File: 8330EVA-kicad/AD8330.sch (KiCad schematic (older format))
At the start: 20 parts, among them J6 Conn_01x03_Male, T1 T1-1T-KK81, T2 T1-1T-KK81, U3 AD8330

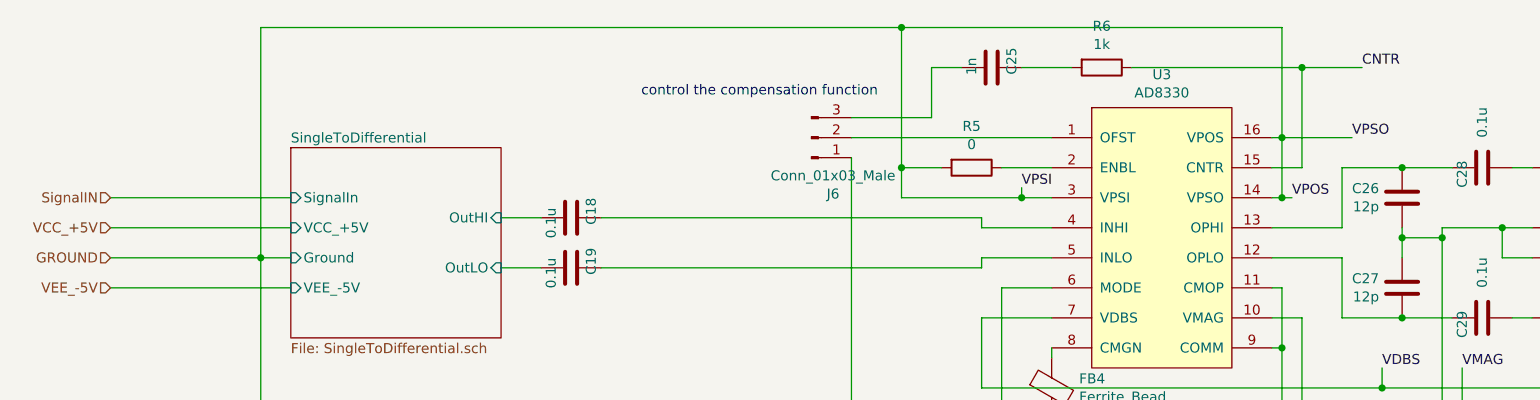
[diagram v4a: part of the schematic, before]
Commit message: 修复AD8330模块中的错误
1.  VCC连接错误
2. VPOS和VPSO标反
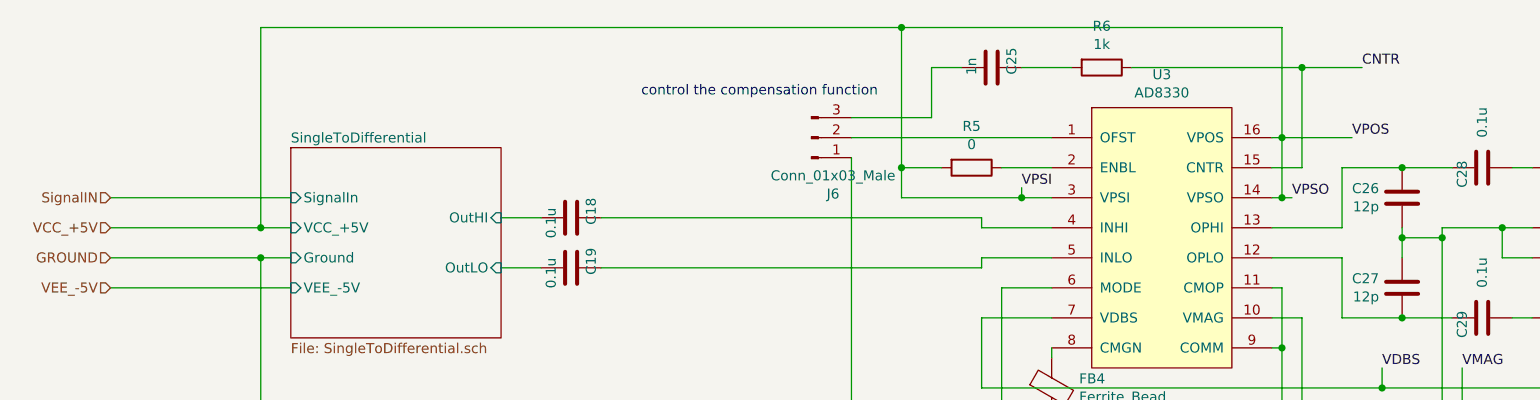
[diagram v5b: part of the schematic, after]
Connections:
- net GROUND: no longer C20.1, C21.1, C22.1, R5.2, U3.14 (VPSO), U3.16 (VPOS), U3.3 (VPSI)
- net VCC_+5V: now also C20.1, C21.1, C22.1, R5.2, U3.14 (VPSO), U3.16 (VPOS), U3.3 (VPSI)
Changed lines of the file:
@@
 	6050 2800 5800 2800
 Text Label 7550 1350 0    50   ~ 0
-VPSO
+VPOS
 Wire Wire Line
 	7550 1350 7200 1350
 Text Label 7250 1650 0    50   ~ 0
-VPOS
+VPSO
 Wire Wire Line
 	7250 1650 7200 1650
@@
 SignalIN
 Wire Wire Line
-	1350 1800 2250 1800
+	1350 1800 2100 1800
 Wire Wire Line
 	1350 1650 2250 1650
 Wire Wire Line
-	2100 1950 2100 800
-Wire Wire Line
 	2100 800  5300 800
 Connection ~ 2100 1950
@@
 Wire Wire Line
 	9700 1800 9900 1800
+Wire Wire Line
+	2100 800  2100 1800
+Connection ~ 2100 1800
+Wire Wire Line
+	2100 1800 2250 1800
 $EndSCHEMATC

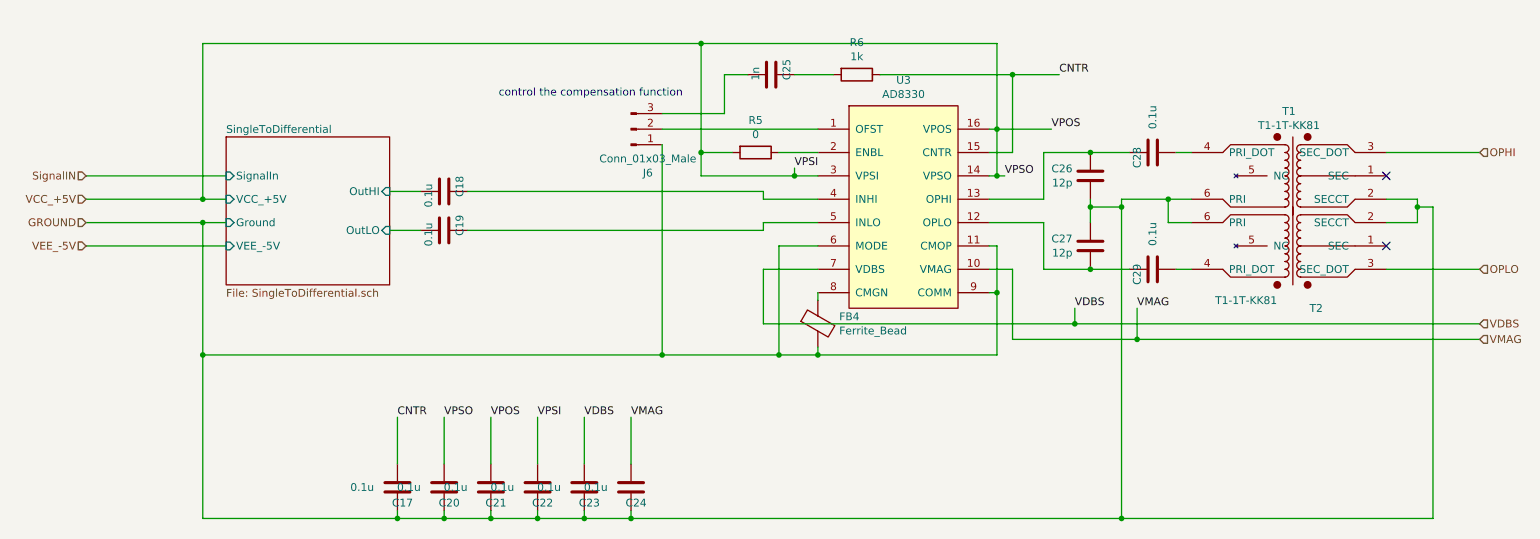
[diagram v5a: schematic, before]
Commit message: 改变巴伦的使用方式
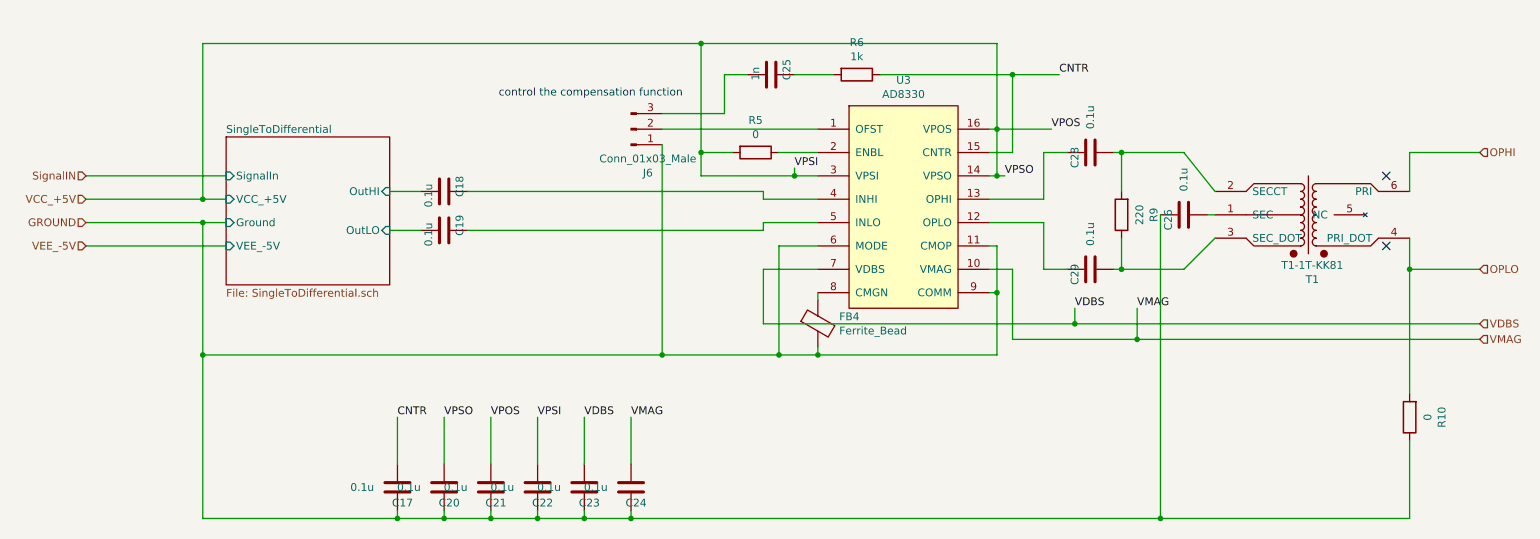
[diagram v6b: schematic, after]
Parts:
- removed C27: 12p, Capacitor_SMD:C_0603_1608Metric_Pad1.05x0.95mm_HandSolder, symbol Device:C
- removed T2: T1-1T-KK81, 8330EVA-footprint-extra:Mini_Circuit_RF_Transformer_SO6, symbol 8330_EVA-extra:T1-1T-KK81
- added R10: 0, Resistor_SMD:R_0805_2012Metric_Pad1.15x1.40mm_HandSolder, symbol Device:R
- added R9: 220, Resistor_SMD:R_0805_2012Metric_Pad1.15x1.40mm_HandSolder, symbol Device:R
- C26: value 12p -> 0.1u
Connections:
- net GROUND: now also C26.2, R10.1; no longer C26.1, T1.2 (SECCT), T1.6 (PRI)
- net OPHI: now also T1.6 (PRI); no longer T1.3 (SEC_DOT)
- net OPLO: now also T1.4 (PRI_DOT), R10.2
- net at C28.2, U3.13 (OPHI): no longer C26.2
- net at T1.1 (SEC): now also C26.1
- net at C28.1: now also T1.2 (SECCT), R9.2; no longer T1.4 (PRI_DOT)
- net at C29.1: now also T1.3 (SEC_DOT), R9.1
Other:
- moved on the sheet: C28, C29, T1
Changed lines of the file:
@@
 	7150 1950 7500 1950
 Wire Wire Line
-	7500 1500 7800 1500
-Wire Wire Line
 	7500 1500 7500 1800
 Wire Wire Line
-	7500 2250 7800 2250
-Wire Wire Line
 	7500 1950 7500 2250
 $Comp
-L Device:C C26
-U 1 1 5BFD0258
-P 7800 1650
-F 0 "C26" H 7685 1604 50  0000 R CNN
-F 1 "12p" H 7685 1695 50  0000 R CNN
-F 2 "Capacitor_SMD:C_0603_1608Metric_Pad1.05x0.95mm_HandSolder" H 7838 1500 50  0001 C CNN
-F 3 "~" H 7800 1650 50  0001 C CNN
-	1    7800 1650
-	1    0    0    1
-$EndComp
-$Comp
-L Device:C C27
-U 1 1 5BFD06D1
-P 7800 2100
-F 0 "C27" H 7685 2054 50  0000 R CNN
-F 1 "12p" H 7685 2145 50  0000 R CNN
-F 2 "Capacitor_SMD:C_0603_1608Metric_Pad1.05x0.95mm_HandSolder" H 7838 1950 50  0001 C CNN
-F 3 "~" H 7800 2100 50  0001 C CNN
-	1    7800 2100
-	1    0    0    1
-$EndComp
-Wire Wire Line
-	7800 1800 7800 1850
-Wire Wire Line
-	8000 1850 7800 1850
-Connection ~ 7800 1850
-Wire Wire Line
-	7800 1850 7800 1950
-$Comp
 L 8330_EVA-extra:T1-1T-KK81 T1
 U 1 1 5BFDF9EF
-P 9100 1650
-F 0 "T1" H 9075 2065 50  0000 C CNN
-F 1 "T1-1T-KK81" H 9075 1974 50  0000 C CNN
-F 2 "8330EVA-footprint-extra:Mini_Circuit_RF_Transformer_SO6" H 9690 1690 50  0001 C CNN
-F 3 "https://ww3.minicircuits.com/pdfs/T1-1T-KK81.pdf" H 9100 1250 50  0001 C CNN
-	1    9100 1650
-	1    0    0    -1
-$EndComp
-$Comp
-L 8330_EVA-extra:T1-1T-KK81 T2
-U 1 1 5BFE14B7
-P 9100 2100
-F 0 "T2" H 9250 2500 50  0000 C CNN
-F 1 "T1-1T-KK81" H 8800 2450 50  0000 C CNN
-F 2 "8330EVA-footprint-extra:Mini_Circuit_RF_Transformer_SO6" H 9690 2140 50  0001 C CNN
-F 3 "https://ww3.minicircuits.com/pdfs/T1-1T-KK81.pdf" H 9100 1700 50  0001 C CNN
-	1    9100 2100
-	1    0    0    1
+P 9200 1900
+F 0 "T1" H 9175 2315 50  0000 C CNN
+F 1 "T1-1T-KK81" H 9175 2224 50  0000 C CNN
+F 2 "8330EVA-footprint-extra:Mini_Circuit_RF_Transformer_SO6" H 9790 1940 50  0001 C CNN
+F 3 "https://ww3.minicircuits.com/pdfs/T1-1T-KK81.pdf" H 9200 1500 50  0001 C CNN
+	1    9200 1900
+	-1   0    0    1
 $EndComp
 Wire Wire Line
-	8450 1800 8300 1800
-Wire Wire Line
-	8000 1800 8000 1850
-Connection ~ 8000 1850
-Wire Wire Line
-	9900 1950 9700 1950
-Wire Wire Line
-	9700 1500 10300 1500
-Wire Wire Line
-	10300 2250 9700 2250
+	10300 2250 9850 2250
 Wire Wire Line
 	7150 2250 7300 2250
@@
 Wire Wire Line
 	3350 3850 3650 3850
-Wire Wire Line
-	8000 3850 4850 3850
 Connection ~ 4850 3850
-Wire Wire Line
-	10000 3850 8000 3850
-Connection ~ 8000 3850
 NoConn ~ 9700 1650
 NoConn ~ 9700 2100
@@
 L Device:C C28
 U 1 1 5C087144
-P 8200 1500
-F 0 "C28" H 8300 1400 50  0000 R CNN
-F 1 "0.1u" H 8050 1500 50  0000 R CNN
-F 2 "Capacitor_SMD:C_0603_1608Metric_Pad1.05x0.95mm_HandSolder" H 8238 1350 50  0001 C CNN
-F 3 "~" H 8200 1500 50  0001 C CNN
-	1    8200 1500
+P 7800 1500
+F 0 "C28" H 7900 1400 50  0000 R CNN
+F 1 "0.1u" H 7650 1500 50  0000 R CNN
+F 2 "Capacitor_SMD:C_0603_1608Metric_Pad1.05x0.95mm_HandSolder" H 7838 1350 50  0001 C CNN
+F 3 "~" H 7800 1500 50  0001 C CNN
+	1    7800 1500
 	0    1    1    0
 $EndComp
-Wire Wire Line
-	8350 1500 8450 1500
-Wire Wire Line
-	8050 1500 7800 1500
-Connection ~ 7800 1500
 $Comp
 L Device:C C29
 U 1 1 5C0A02D1
-P 8200 2250
-F 0 "C29" H 8300 2150 50  0000 R CNN
-F 1 "0.1u" H 8050 2250 50  0000 R CNN
-F 2 "Capacitor_SMD:C_0603_1608Metric_Pad1.05x0.95mm_HandSolder" H 8238 2100 50  0001 C CNN
-F 3 "~" H 8200 2250 50  0001 C CNN
-	1    8200 2250
+P 7800 2250
+F 0 "C29" H 7900 2150 50  0000 R CNN
+F 1 "0.1u" H 7650 2250 50  0000 R CNN
+F 2 "Capacitor_SMD:C_0603_1608Metric_Pad1.05x0.95mm_HandSolder" H 7838 2100 50  0001 C CNN
+F 3 "~" H 7800 2250 50  0001 C CNN
+	1    7800 2250
 	0    1    1    0
 $EndComp
-Wire Wire Line
-	8350 2250 8450 2250
-Wire Wire Line
-	8050 2250 7800 2250
-Connection ~ 7800 2250
-Wire Wire Line
-	9900 1800 9900 1850
-Wire Wire Line
-	10000 1850 9900 1850
-Wire Wire Line
-	10000 1850 10000 3850
-Connection ~ 9900 1850
-Wire Wire Line
-	9900 1850 9900 1950
-Wire Wire Line
-	8000 1850 8000 3850
-Wire Wire Line
-	8450 1950 8300 1950
-Wire Wire Line
-	8300 1950 8300 1800
-Connection ~ 8300 1800
-Wire Wire Line
-	8300 1800 8000 1800
 $Bitmap
 Pos 3900 6000
@@
 $EndBitmap
 Wire Wire Line
-	9700 1800 9900 1800
-Wire Wire Line
 	2100 800  2100 1800
 Connection ~ 2100 1800
 Wire Wire Line
 	2100 1800 2250 1800
+Wire Wire Line
+	7500 2250 7650 2250
+Wire Wire Line
+	7500 1500 7650 1500
+Wire Wire Line
+	4850 3850 8250 3850
+$Comp
+L Device:C C26
+U 1 1 5BFEEF3F
+P 8400 1900
+F 0 "C26" H 8500 1800 50  0000 R CNN
+F 1 "0.1u" H 8250 1900 50  0000 R CNN
+F 2 "Capacitor_SMD:C_0603_1608Metric_Pad1.05x0.95mm_HandSolder" H 8438 1750 50  0001 C CNN
+F 3 "~" H 8400 1900 50  0001 C CNN
+	1    8400 1900
+	0    1    1    0
+$EndComp
+Wire Wire Line
+	7950 2250 8000 2250
+Wire Wire Line
+	8400 2250 8600 2050
+Wire Wire Line
+	8400 1500 8600 1750
+Wire Wire Line
+	7950 1500 8000 1500
+Wire Wire Line
+	8550 1900 8600 1900
+Wire Wire Line
+	8250 1900 8250 3850
+Connection ~ 8250 3850
+Wire Wire Line
+	8250 3850 9850 3850
+$Comp
+L Device:R R9
+U 1 1 5C01052F
+P 8000 1900
+F 0 "R9" V 7793 1900 50  0000 C CNN
+F 1 "220" V 7884 1900 50  0000 C CNN
+F 2 "Resistor_SMD:R_0805_2012Metric_Pad1.15x1.40mm_HandSolder" V 7930 1900 50  0001 C CNN
+F 3 "~" H 8000 1900 50  0001 C CNN
+	1    8000 1900
+	-1   0    0    1
+$EndComp
+Wire Wire Line
+	8000 1750 8000 1500
+Connection ~ 8000 1500
+Wire Wire Line
+	8000 1500 8400 1500
+Wire Wire Line
+	8000 2050 8000 2250
+Connection ~ 8000 2250
+Wire Wire Line
+	8000 2250 8400 2250
+Wire Wire Line
+	9850 1500 9850 1750
+Wire Wire Line
+	9850 1500 10300 1500
+Connection ~ 9850 2250
+$Comp
+L Device:R R10
+U 1 1 5C02A3FB
+P 9850 3200
+F 0 "R10" V 9643 3200 50  0000 C CNN
+F 1 "0" V 9734 3200 50  0000 C CNN
+F 2 "Resistor_SMD:R_0805_2012Metric_Pad1.15x1.40mm_HandSolder" V 9780 3200 50  0001 C CNN
+F 3 "~" H 9850 3200 50  0001 C CNN
+	1    9850 3200
+	-1   0    0    1
+$EndComp
+Wire Wire Line
+	9850 2250 9850 3050
+Wire Wire Line
+	9850 3350 9850 3850
+Wire Wire Line
+	9850 2050 9850 2250
 $EndSCHEMATC
